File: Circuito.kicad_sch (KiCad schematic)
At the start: 14 parts, among them J1 Raspberry_Pi, Q1 BSS138, Q2 BSS138, Q3 BSS138, U1 DHT11, U2 BMP280_I2C

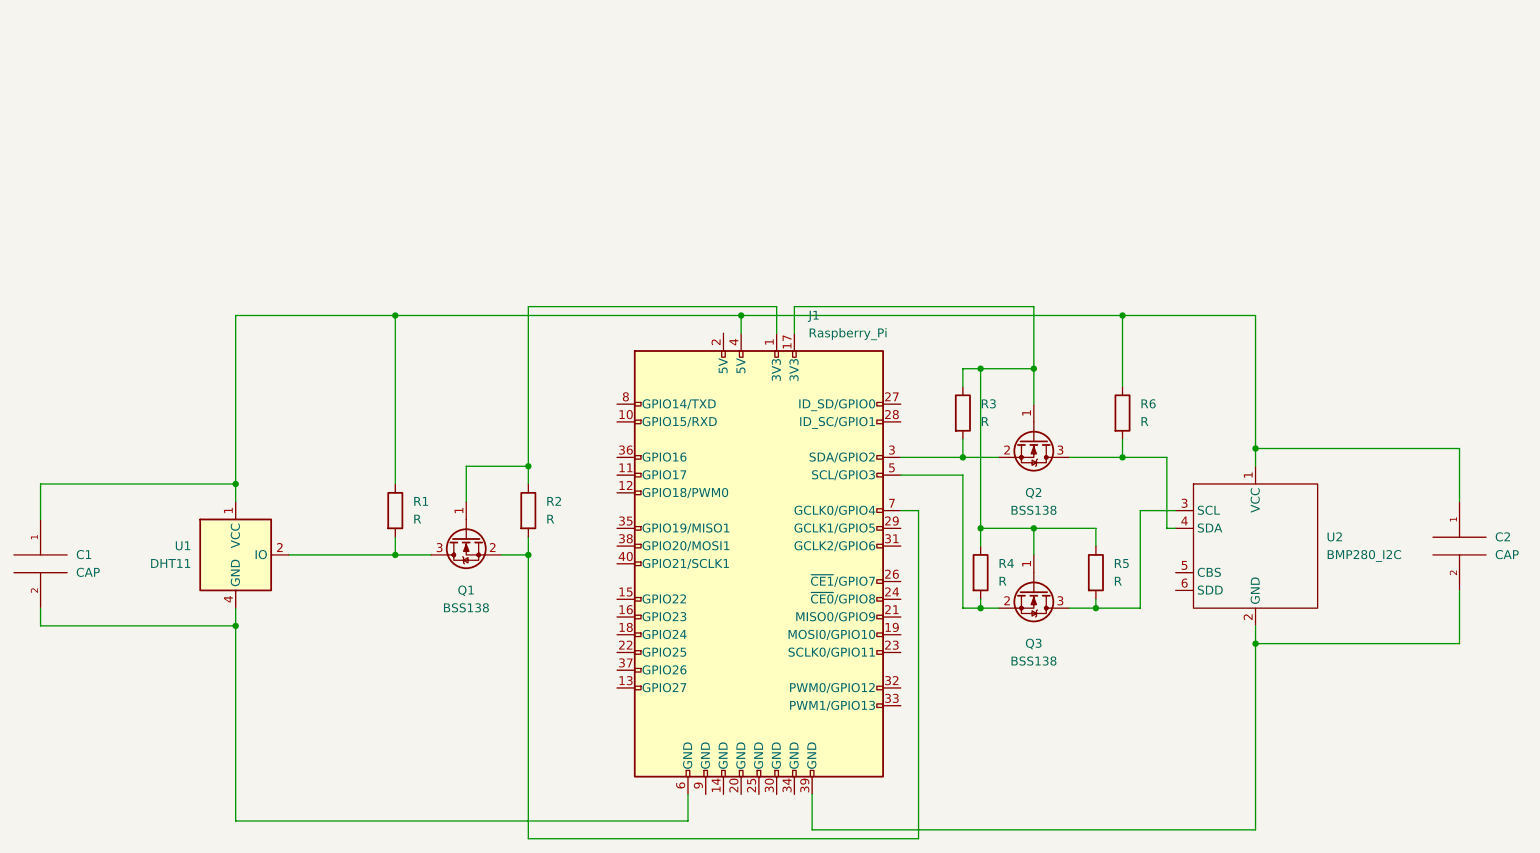
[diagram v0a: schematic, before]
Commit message: Se cambian los MOSFET
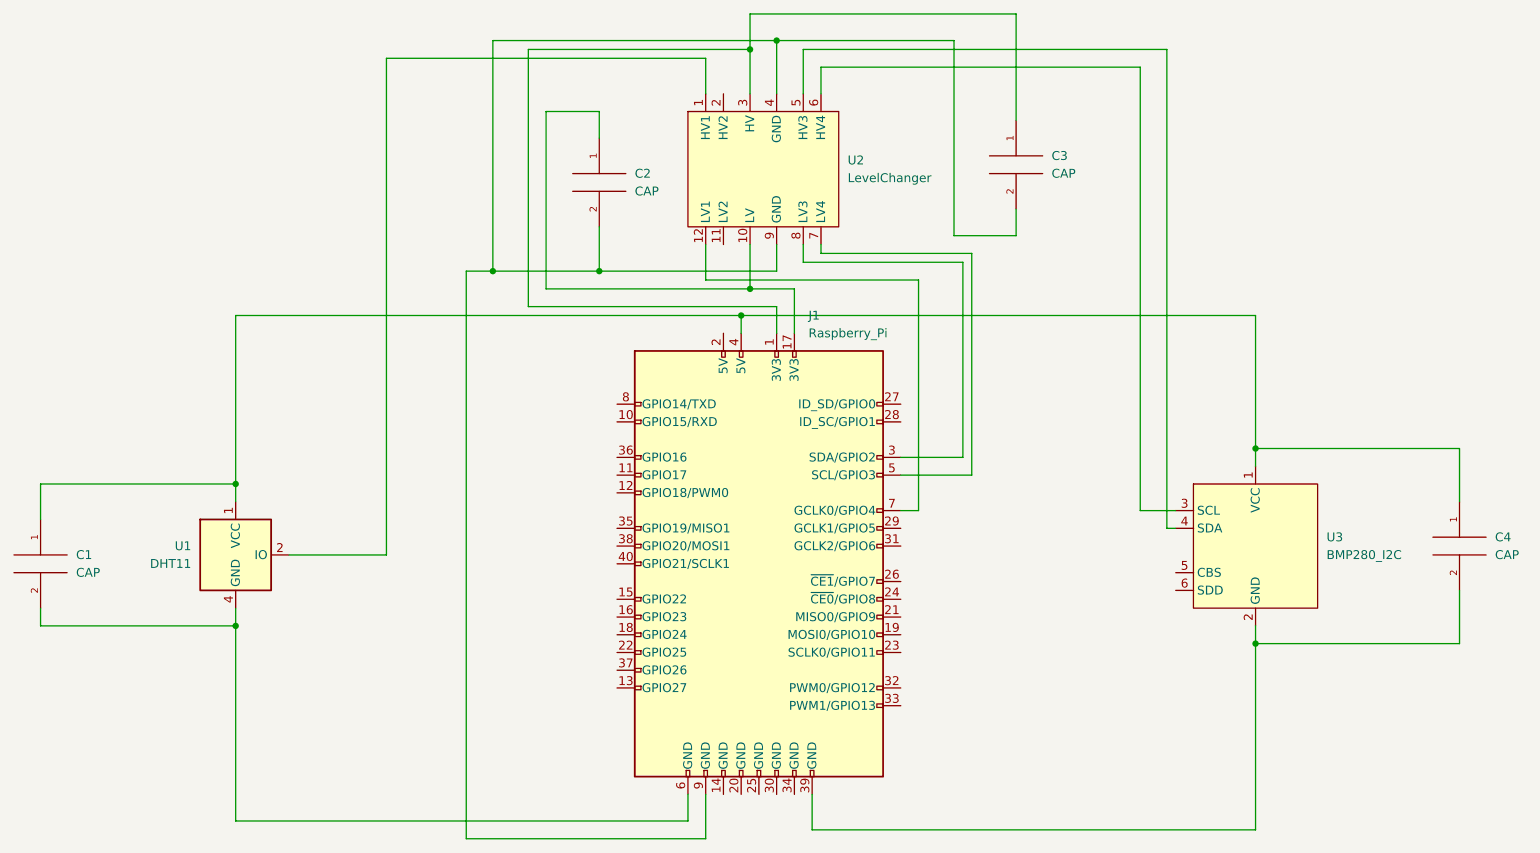
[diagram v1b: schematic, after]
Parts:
- removed Q1, Q2, Q3: BSS138, Package_TO_SOT_SMD:SOT-23, symbol Transistor_FET:BSS138
- removed R1, R2, R3, R4, R5, R6: R, symbol Device:R
- removed U2: BMP280_I2C, symbol Custom2:BMP280_I2C
- added C2, C3: CAP, symbol pspice:CAP
- added U2: LevelChanger, symbol Custom2:LevelChanger
- added U3: BMP280_I2C, symbol Custom2:BMP280_I2C
- renumbered C2 to C4
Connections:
- net at J1.17 (3V3): now also C2.1, U2.10 (LV)
- net at C1.1, C4.1, J1.4 (5V)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: now also U3.1 (VCC)
- net at U1.2 (IO): now also U2.1 (HV1)
- net at J1.5 (SCL/GPIO3): now also U2.7 (LV4)
- net at J1.3 (SDA/GPIO2): now also U2.8 (LV3)
- net at J1.1 (3V3): now also C3.1, U2.3 (HV)
- net at C4.2, J1.39 (GND): now also U3.2 (GND)
- net at J1.7 (GCLK0/GPIO4): now also U2.12 (LV1)
- net at J1.9 (GND): now also C2.2, C3.2, U2.4 (GND), U2.9 (GND)
- new net: U2.5 (HV3), U3.4 (SDA)
- new net: U2.6 (HV4), U3.3 (SCL)

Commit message: Se cambia DHT11 por DHT22
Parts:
- removed U1: DHT11, Sensor:Aosong_DHT11_5.5x12.0_P2.54mm, symbol Sensor:DHT11
- added U1: DHT22, symbol Custom2:DHT22
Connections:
- net at C1.1, C4.1, J1.4 (5V)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: now also U1.1 (VDD)
- net at C1.2, J1.6 (GND): now also U1.4 (GND)
- net at U2.1 (HV1): now also U1.2 (DATA)
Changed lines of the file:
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@@
   (junction (at 121.92 59.69) (diameter 0) (color 0 0 0 0)
   )
+  (junction (at 162.56 26.67) (diameter 0) (color 0 0 0 0)
+  )
   (junction (at 85.09 90.17) (diameter 0) (color 0 0 0 0)
   )
-  (junction (at 162.56 26.67) (diameter 0) (color 0 0 0 0)
-  )
   (junction (at 85.09 110.49) (diameter 0) (color 0 0 0 0)
   )
@@
     (stroke (width 0) (type default) (color 0 0 0 0))
   )
-  (wire (pts (xy 106.68 29.21) (xy 106.68 100.33))
+  (wire (pts (xy 106.68 29.21) (xy 106.68 99.06))
     (stroke (width 0) (type default) (color 0 0 0 0))
   )
@@
     (stroke (width 0) (type default) (color 0 0 0 0))
   )
+  (wire (pts (xy 85.09 96.52) (xy 85.09 90.17))
+    (stroke (width 0) (type default) (color 0 0 0 0))
+  )
   (wire (pts (xy 218.44 27.94) (xy 166.37 27.94))
     (stroke (width 0) (type default) (color 0 0 0 0))
@@
     (stroke (width 0) (type default) (color 0 0 0 0))
   )
-  (wire (pts (xy 85.09 92.71) (xy 85.09 90.17))
-    (stroke (width 0) (type default) (color 0 0 0 0))
-  )
   (wire (pts (xy 189.23 86.36) (xy 189.23 58.42))
     (stroke (width 0) (type default) (color 0 0 0 0))
@@
     (stroke (width 0) (type default) (color 0 0 0 0))
   )
-  (wire (pts (xy 85.09 110.49) (xy 85.09 107.95))
-    (stroke (width 0) (type default) (color 0 0 0 0))
-  )
   (wire (pts (xy 218.44 27.94) (xy 218.44 96.52))
     (stroke (width 0) (type default) (color 0 0 0 0))
@@
     (stroke (width 0) (type default) (color 0 0 0 0))
   )
-  (wire (pts (xy 92.71 100.33) (xy 106.68 100.33))
-    (stroke (width 0) (type default) (color 0 0 0 0))
-  )
   (wire (pts (xy 168.91 34.29) (xy 168.91 30.48))
     (stroke (width 0) (type default) (color 0 0 0 0))
@@
     (stroke (width 0) (type default) (color 0 0 0 0))
   )
+  (wire (pts (xy 83.82 104.14) (xy 85.09 104.14))
+    (stroke (width 0) (type default) (color 0 0 0 0))
+  )
   (wire (pts (xy 158.75 27.94) (xy 158.75 22.86))
     (stroke (width 0) (type default) (color 0 0 0 0))
@@
     (stroke (width 0) (type default) (color 0 0 0 0))
   )
+  (wire (pts (xy 83.82 96.52) (xy 85.09 96.52))
+    (stroke (width 0) (type default) (color 0 0 0 0))
+  )
   (wire (pts (xy 189.23 58.42) (xy 166.37 58.42))
     (stroke (width 0) (type default) (color 0 0 0 0))
@@
     (stroke (width 0) (type default) (color 0 0 0 0))
   )
+  (wire (pts (xy 85.09 104.14) (xy 85.09 110.49))
+    (stroke (width 0) (type default) (color 0 0 0 0))
+  )
   (wire (pts (xy 168.91 57.15) (xy 190.5 57.15))
     (stroke (width 0) (type default) (color 0 0 0 0))
@@
     (stroke (width 0) (type default) (color 0 0 0 0))
   )
+  (wire (pts (xy 83.82 99.06) (xy 106.68 99.06))
+    (stroke (width 0) (type default) (color 0 0 0 0))
+  )
   (wire (pts (xy 231.14 85.09) (xy 260.35 85.09))
     (stroke (width 0) (type default) (color 0 0 0 0))
@@
   (wire (pts (xy 162.56 64.77) (xy 127 64.77))
     (stroke (width 0) (type default) (color 0 0 0 0))
+  )
+  (symbol (lib_id "Custom2:DHT22") (at 76.2 100.33 90) (mirror x) (unit 1)
+    (in_bom yes) (on_board yes) (fields_autoplaced)
+    (property "Reference" "U1" (id 0) (at 76.2 88.9 90))
+    (property "Value" "DHT22" (id 1) (at 76.2 91.44 90))
+    (property "Footprint" "" (id 2) (at 76.2 100.33 0)
+      (effects (font (size 1.27 1.27)) hide)
+    )
+    (property "Datasheet" "" (id 3) (at 76.2 100.33 0)
+      (effects (font (size 1.27 1.27)) hide)
+    )
+    (pin "1")
+    (pin "2")
+    (pin "3")
+    (pin "4")
   )
   (symbol (lib_id "pspice:CAP") (at 137.16 46.99 0) (unit 1)
@@
     (pin "9")
   )
-  (symbol (lib_id "Sensor:DHT11") (at 85.09 100.33 0) (unit 1)
-    (in_bom yes) (on_board yes) (fields_autoplaced)
-    (property "Reference" "U1" (id 0) (at 78.74 99.0599 0)
-      (effects (font (size 1.27 1.27)) (justify right))
-    )
-    (property "Value" "DHT11" (id 1) (at 78.74 101.5999 0)
-      (effects (font (size 1.27 1.27)) (justify right))
-    )
-    (property "Footprint" "Sensor:Aosong_DHT11_5.5x12.0_P2.54mm" (id 2) (at 85.09 110.49 0)
-      (effects (font (size 1.27 1.27)) hide)
-    )
-    (property "Datasheet" "http://akizukidenshi.com/download/ds/aosong/DHT11.pdf" (id 3) (at 88.9 93.98 0)
-      (effects (font (size 1.27 1.27)) hide)
-    )
-    (pin "1")
-    (pin "2")
-    (pin "3")
-    (pin "4")
-  )
   (symbol (lib_id "Custom2:BMP280_I2C") (at 231.14 99.06 0) (unit 1)
     (in_bom yes) (on_board yes) (fields_autoplaced)
@@
       (reference "J1") (unit 1) (value "Raspberry_Pi") (footprint "")
     )
-    (path "/e1e708ba-caba-4519-94a2-17f6e949ea23"
-      (reference "U1") (unit 1) (value "DHT11") (footprint "Sensor:Aosong_DHT11_5.5x12.0_P2.54mm")
+    (path "/5de8539b-452c-469e-b52d-30dfcb8b6380"
+      (reference "U1") (unit 1) (value "DHT22") (footprint "")
     )
     (path "/c18f2965-bf6f-4805-b1c3-e0226cdc7880"
